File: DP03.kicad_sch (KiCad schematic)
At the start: 21 parts

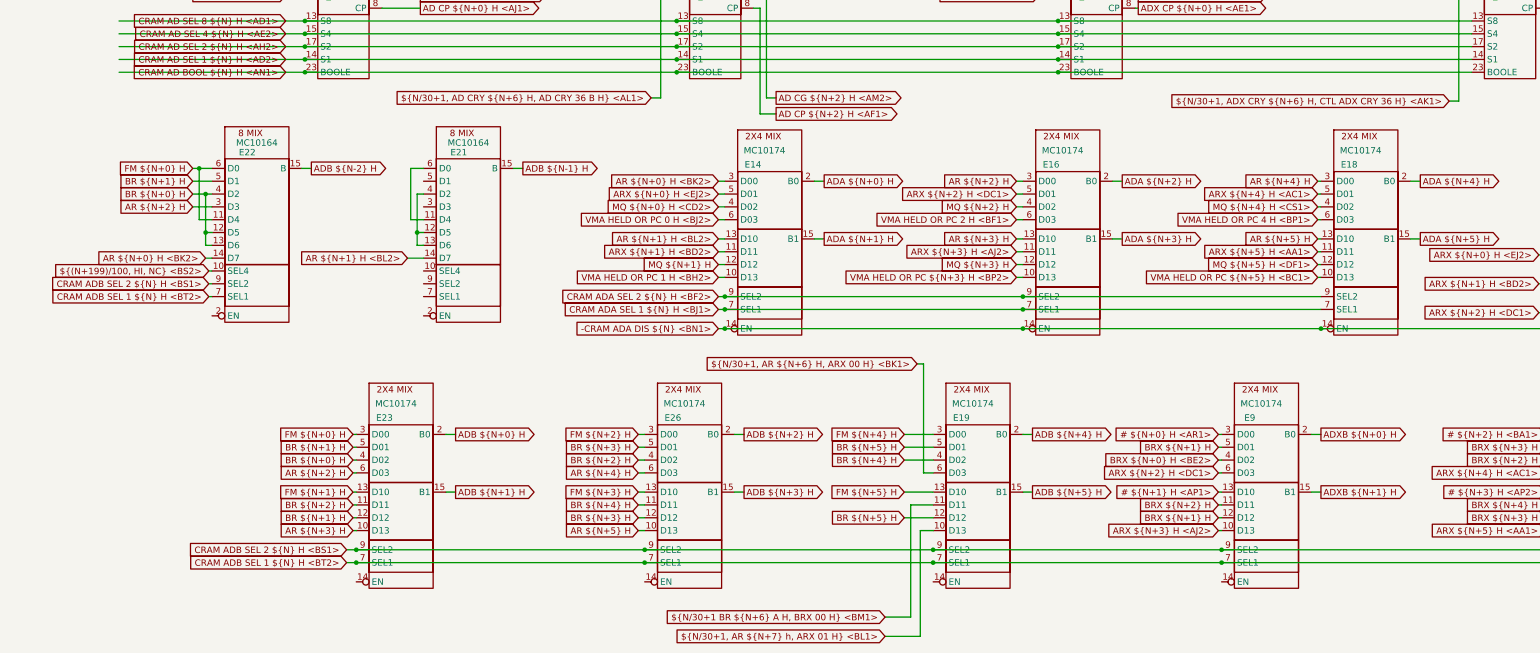
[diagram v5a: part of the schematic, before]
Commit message: Parser is greedily eating characters up to next "}" instead of following nesting. Fix lowercase "h" found in some signal names. Add error message stuff for signal name syntax errors.
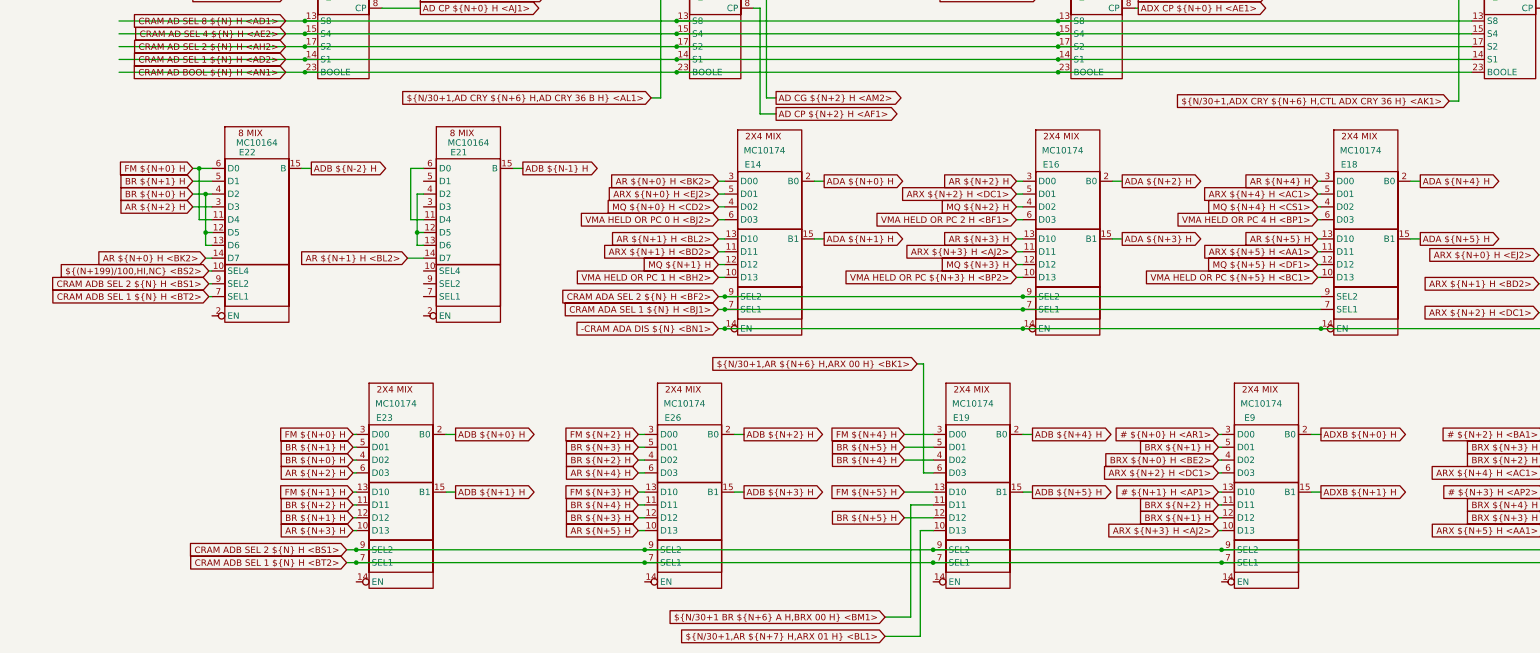
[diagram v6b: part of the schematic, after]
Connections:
- net ${(N+199)/100, HI, NC} <BS2> renamed ${(N+199)/100,HI,NC} <BS2>
- net ${N/30+1 BR ${N+6} A H, BRX 00 H} <BM1> renamed ${N/30+1 BR ${N+6} A H,BRX 00 H} <BM1>
- net ${N/30+1, AD CRY ${N+6} H, AD CRY 36 B H} <AL1> renamed ${N/30+1,AD CRY ${N+6} H,AD CRY 36 B H} <AL1>
- net ${N/30+1, ADX CRY ${N+6} H, CTL ADX CRY 36 H} <AK1> renamed ${N/30+1,ADX CRY ${N+6} H,CTL ADX CRY 36 H} <AK1>
- net ${N/30+1, AR ${N+6} H, ARX 00 H} <BK1> renamed ${N/30+1,AR ${N+6} H,ARX 00 H} <BK1>
- net ${N/30+1, AR ${N+7} h, ARX 01 H} <BL1> renamed ${N/30+1,AR ${N+7} H,ARX 01 H} <BL1>
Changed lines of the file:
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@@
     )
   )
-  (global_label "${N/30+1, AR ${N+7} h, ARX 01 H} <BL1>" (shape input) (at 184.785 234.95 180) (fields_autoplaced)
-    (effects (font (size 1.27 1.27)) (justify right))
-    (property "Intersheet References" "${INTERSHEET_REFS}" (id 0) (at 133.749 234.8706 0)
+  (global_label "${N{slash}30+1,AR ${N+7} H,ARX 01 H} <BL1>" (shape input) (at 184.785 234.95 180) (fields_autoplaced)
+    (effects (font (size 1.27 1.27)) (justify right))
+    (property "Intersheet References" "${INTERSHEET_REFS}" (id 0) (at 135.5029 234.8706 0)
       (effects (font (size 1.27 1.27)) (justify right) hide)
     )
@@
     )
   )
-  (global_label "${N/30+1 BR ${N+6} A H, BRX 00 H} <BM1>" (shape input) (at 184.785 231.14 180) (fields_autoplaced)
+  (global_label "${N/30+1 BR ${N+6} A H,BRX 00 H} <BM1>" (shape input) (at 184.785 231.14 180) (fields_autoplaced)
     (effects (font (size 1.27 1.27)) (justify right))
     (property "Intersheet References" "${INTERSHEET_REFS}" (id 0) (at 131.33 231.0606 0)
@@
     )
   )
-  (global_label "${N/30+1, AD CRY ${N+6} H, AD CRY 36 B H} <AL1>" (shape input) (at 138.43 128.27 180) (fields_autoplaced)
+  (global_label "${N/30+1,AD CRY ${N+6} H,AD CRY 36 B H} <AL1>" (shape input) (at 138.43 128.27 180) (fields_autoplaced)
     (effects (font (size 1.27 1.27)) (justify right))
     (property "Intersheet References" "${INTERSHEET_REFS}" (id 0) (at 77.1736 128.1906 0)
@@
     )
   )
-  (global_label "${(N+199)/100, HI, NC} <BS2>" (shape input) (at 50.8 162.56 180) (fields_autoplaced)
+  (global_label "${(N+199)/100,HI,NC} <BS2>" (shape input) (at 50.8 162.56 180) (fields_autoplaced)
     (effects (font (size 1.27 1.27)) (justify right))
     (property "Intersheet References" "${INTERSHEET_REFS}" (id 0) (at 11.4359 162.4806 0)
@@
     )
   )
-  (global_label "${N/30+1, AR ${N+6} H, ARX 00 H} <BK1>" (shape input) (at 191.135 180.975 180) (fields_autoplaced)
+  (global_label "${N/30+1,AR ${N+6} H,ARX 00 H} <BK1>" (shape input) (at 191.135 180.975 180) (fields_autoplaced)
     (effects (font (size 1.27 1.27)) (justify right))
     (property "Intersheet References" "${INTERSHEET_REFS}" (id 0) (at 139.6757 180.8956 0)
@@
     )
   )
-  (global_label "${N/30+1, ADX CRY ${N+6} H, CTL ADX CRY 36 H} <AK1>" (shape input)
-    (at 296.545 128.905 0) (fields_autoplaced)
+  (global_label "${N/30+1,ADX CRY ${N+6} H,CTL ADX CRY 36 H} <AK1>" (shape input) (at 296.545 128.905 0) (fields_autoplaced)
     (effects (font (size 1.27 1.27)) (justify right))
     (property "Intersheet References" "${INTERSHEET_REFS}" (id 0) (at 230.6319 128.8256 0)
